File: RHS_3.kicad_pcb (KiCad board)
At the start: 2 copper layers, 51 x 61 mm, 64 parts, among them IC1 ATMEGA328P-A, IC2 CC1101, IC3 CC1101_Chip, J1 Glass Breakage Detector, J2 ANT, P4 ISP Bottom, P5 ISP Top, P6 FTDI, P7 ISP 10, SW1 Reset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

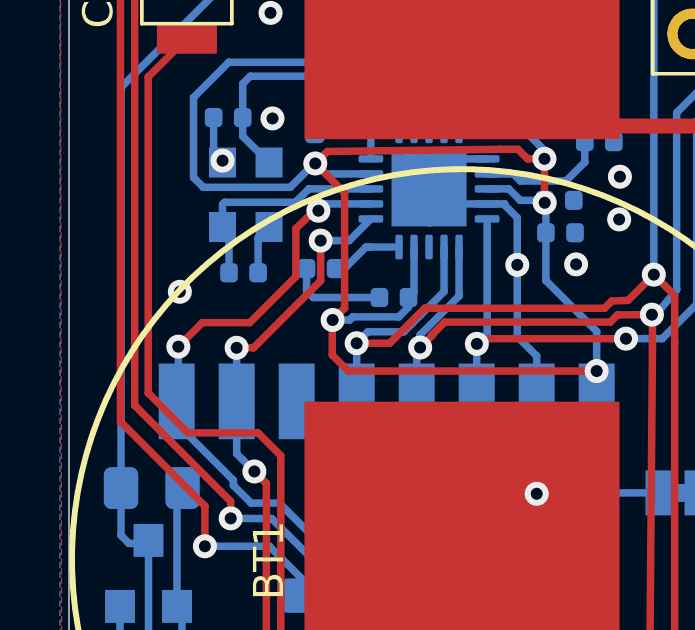
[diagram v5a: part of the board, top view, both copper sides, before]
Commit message: layout changed
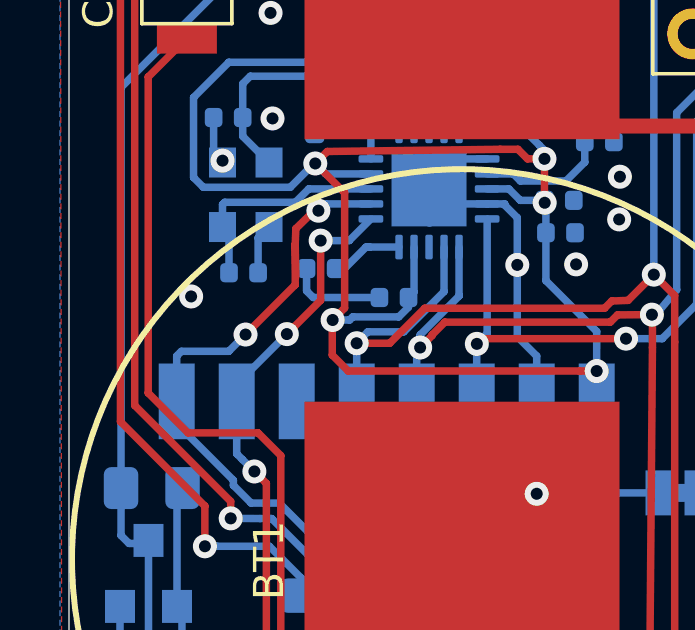
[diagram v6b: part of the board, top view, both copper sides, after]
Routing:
- net /CS: track 31.1 -> 32.3 mm
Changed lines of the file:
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@@
     (thickness 1.6)
     (drawings 33)
-    (tracks 713)
+    (tracks 717)
     (zones 0)
     (modules 64)
@@
     (tags "solder jumper open")
     (attr virtual)
-    (fp_text reference JP2 (at 0 1.8) (layer B.SilkS)
+    (fp_text reference JP2 (at 3.0734 -0.01016) (layer B.SilkS)
       (effects (font (size 1 1) (thickness 0.15)) (justify mirror))
     )
@@
   (segment (start 71.501 88.1888) (end 71.5137 88.2015) (width 0.25) (layer B.Cu) (net 2))
   (segment (start 71.501 87.0585) (end 71.501 87.1093) (width 0.25) (layer B.Cu) (net 2))
-  (via (at 63.1952 90.4875) (size 0.8) (drill 0.4) (layers F.Cu B.Cu) (net 2))
+  (via (at 63.57112 90.64244) (size 0.8) (drill 0.4) (layers F.Cu B.Cu) (net 2))
   (via (at 77.8637 86.6521) (size 0.8) (drill 0.4) (layers F.Cu B.Cu) (net 2))
   (via (at 77.8383 88.0745) (size 0.8) (drill 0.4) (layers F.Cu B.Cu) (net 2))
@@
   (segment (start 69.68 99.03) (end 70.7 100.05) (width 0.25) (layer B.Cu) (net 34))
   (segment (start 71.423599 103.520009) (end 71.796401 103.520009) (width 0.25) (layer B.Cu) (net 34))
-  (via (at 63.1444 92.3163) (size 0.8) (drill 0.4) (layers F.Cu B.Cu) (net 34))
+  (via (at 65.38468 91.91244) (size 0.8) (drill 0.4) (layers F.Cu B.Cu) (net 34))
   (segment (start 63.1444 94.0856) (end 63.09 94.14) (width 0.25) (layer B.Cu) (net 34))
-  (segment (start 63.1444 92.3163) (end 63.1444 94.0856) (width 0.25) (layer B.Cu) (net 34))
   (segment (start 68.038345 87.5585) (end 67.813335 87.78351) (width 0.25) (layer B.Cu) (net 34))
   (segment (start 69.5635 87.5585) (end 68.038345 87.5585) (width 0.25) (layer B.Cu) (net 34))
   (segment (start 67.813335 87.761653) (end 67.813335 87.78351) (width 0.25) (layer B.Cu) (net 34))
   (segment (start 67.67719 87.78351) (end 67.813335 87.78351) (width 0.25) (layer F.Cu) (net 34))
-  (via (at 67.813335 87.78351) (size 0.8) (drill 0.4) (layers F.Cu B.Cu) (net 34))
+  (via (at 67.813335 87.78351) (size 0.8) (drill 0.4) (layers F.Cu B.Cu) (net 34) (status 1000000))
   (segment (start 67.866488 87.7085) (end 67.813335 87.761653) (width 0.25) (layer B.Cu) (net 34))
-  (segment (start 63.94577 91.51493) (end 65.52819 91.51493) (width 0.25) (layer F.Cu) (net 34))
-  (segment (start 63.1444 92.3163) (end 63.94577 91.51493) (width 0.25) (layer F.Cu) (net 34))
-  (segment (start 67.06108 89.98204) (end 67.06108 88.38184) (width 0.25) (layer F.Cu) (net 34))
-  (segment (start 65.52819 91.51493) (end 67.06108 89.98204) (width 0.25) (layer F.Cu) (net 34))
   (segment (start 67.06108 88.38184) (end 67.67719 87.78351) (width 0.25) (layer F.Cu) (net 34))
+  (segment (start 67.06108 89.98204) (end 67.04076 88.90508) (width 0.25) (layer F.Cu) (net 34))
+  (segment (start 67.04076 88.90508) (end 67.06108 88.38184) (width 0.25) (layer F.Cu) (net 34))
+  (segment (start 63.24676 92.47124) (end 64.82588 92.47124) (width 0.25) (layer B.Cu) (net 34))
+  (segment (start 63.09 94.14) (end 63.09 92.628) (width 0.25) (layer B.Cu) (net 34))
+  (segment (start 64.82588 92.47124) (end 65.38468 91.91244) (width 0.25) (layer B.Cu) (net 34))
+  (segment (start 63.09 92.628) (end 63.24676 92.47124) (width 0.25) (layer B.Cu) (net 34))
+  (segment (start 67.04076 90.25636) (end 65.38468 91.91244) (width 0.25) (layer F.Cu) (net 34))
+  (segment (start 67.04076 88.90508) (end 67.04076 90.25636) (width 0.25) (layer F.Cu) (net 34))
   (segment (start 71.84 113.3) (end 71.84 110.652354) (width 0.25) (layer B.Cu) (net 35))
   (via (at 72.015431 110.476923) (size 0.8) (drill 0.4) (layers F.Cu B.Cu) (net 35))
@@
   (via (at 65.67971 96.476464) (size 0.8) (drill 0.4) (layers F.Cu B.Cu) (net 35))
   (segment (start 65.09 94.14) (end 65.09 95.886754) (width 0.25) (layer B.Cu) (net 35))
-  (via (at 65.0875 92.3544) (size 0.8) (drill 0.4) (layers F.Cu B.Cu) (net 35))
+  (via (at 66.76136 91.8972) (size 0.8) (drill 0.4) (layers F.Cu B.Cu) (net 35))
   (segment (start 65.0875 94.1375) (end 65.09 94.14) (width 0.25) (layer B.Cu) (net 35))
-  (segment (start 65.0875 92.3544) (end 65.0875 94.1375) (width 0.25) (layer B.Cu) (net 35))
   (segment (start 69.5635 88.0585) (end 68.841314 88.780686) (width 0.25) (layer B.Cu) (net 35))
   (via (at 67.888589 88.780686) (size 0.8) (drill 0.4) (layers F.Cu B.Cu) (net 35))
   (segment (start 68.841314 88.780686) (end 67.888589 88.780686) (width 0.25) (layer B.Cu) (net 35))
-  (segment (start 67.888589 90.118996) (end 67.888589 89.346371) (width 0.25) (layer F.Cu) (net 35))
-  (segment (start 67.888589 89.346371) (end 67.888589 88.780686) (width 0.25) (layer F.Cu) (net 35))
-  (segment (start 65.653185 92.3544) (end 67.888589 90.118996) (width 0.25) (layer F.Cu) (net 35))
-  (segment (start 65.0875 92.3544) (end 65.653185 92.3544) (width 0.25) (layer F.Cu) (net 35))
+  (segment (start 65.09 93.478) (end 65.09 94.14) (width 0.25) (layer B.Cu) (net 35))
+  (segment (start 65.09 94.14) (end 65.09 93.41108) (width 0.25) (layer B.Cu) (net 35))
+  (segment (start 65.24748 93.41108) (end 66.76136 91.8972) (width 0.25) (layer B.Cu) (net 35))
+  (segment (start 65.09 93.41108) (end 65.24748 93.41108) (width 0.25) (layer B.Cu) (net 35))
+  (segment (start 67.888589 90.769971) (end 66.76136 91.8972) (width 0.25) (layer F.Cu) (net 35))
+  (segment (start 67.888589 88.780686) (end 67.888589 90.769971) (width 0.25) (layer F.Cu) (net 35))
   (segment (start 71.001 83.805) (end 70.5485 83.3525) (width 0.25) (layer B.Cu) (net 37))
   (segment (start 71.001 85.121) (end 71.001 83.805) (width 0.25) (layer B.Cu) (net 37))

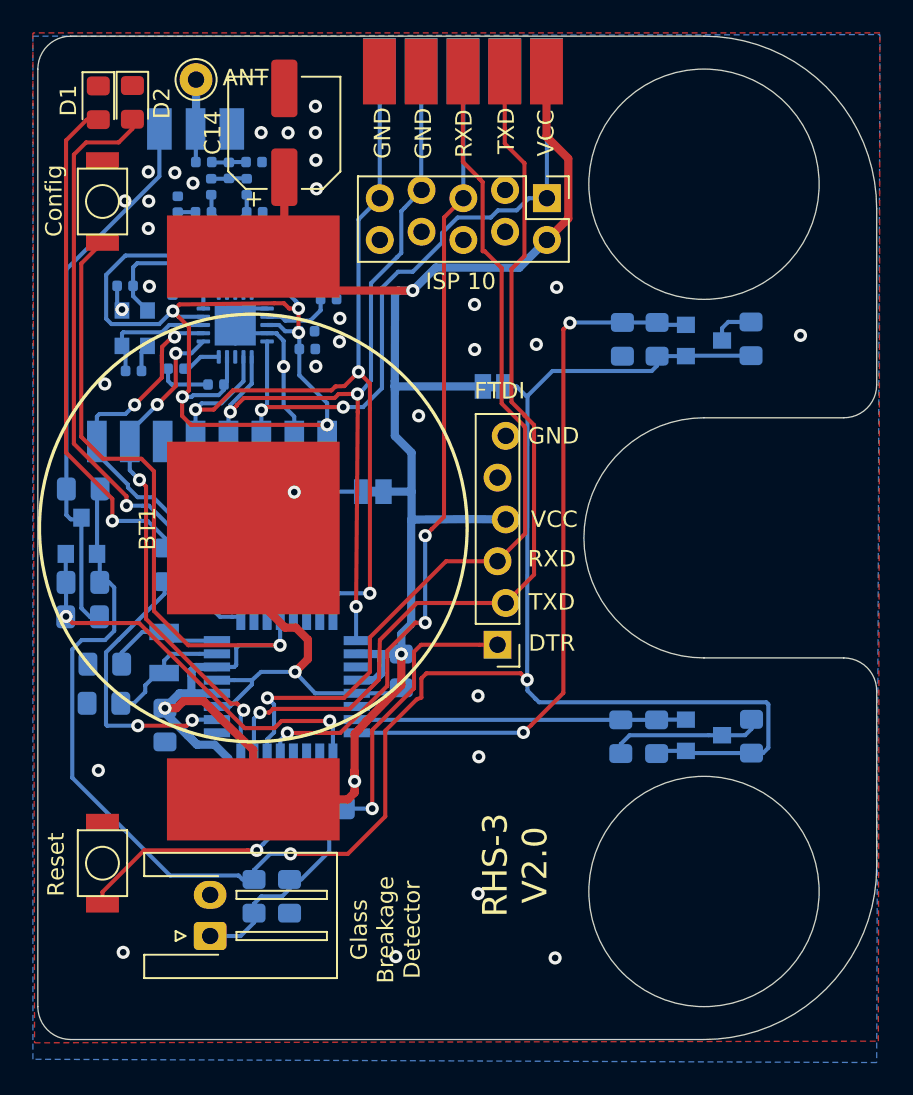
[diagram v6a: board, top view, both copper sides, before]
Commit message: switches for TLEs & CC1101 added
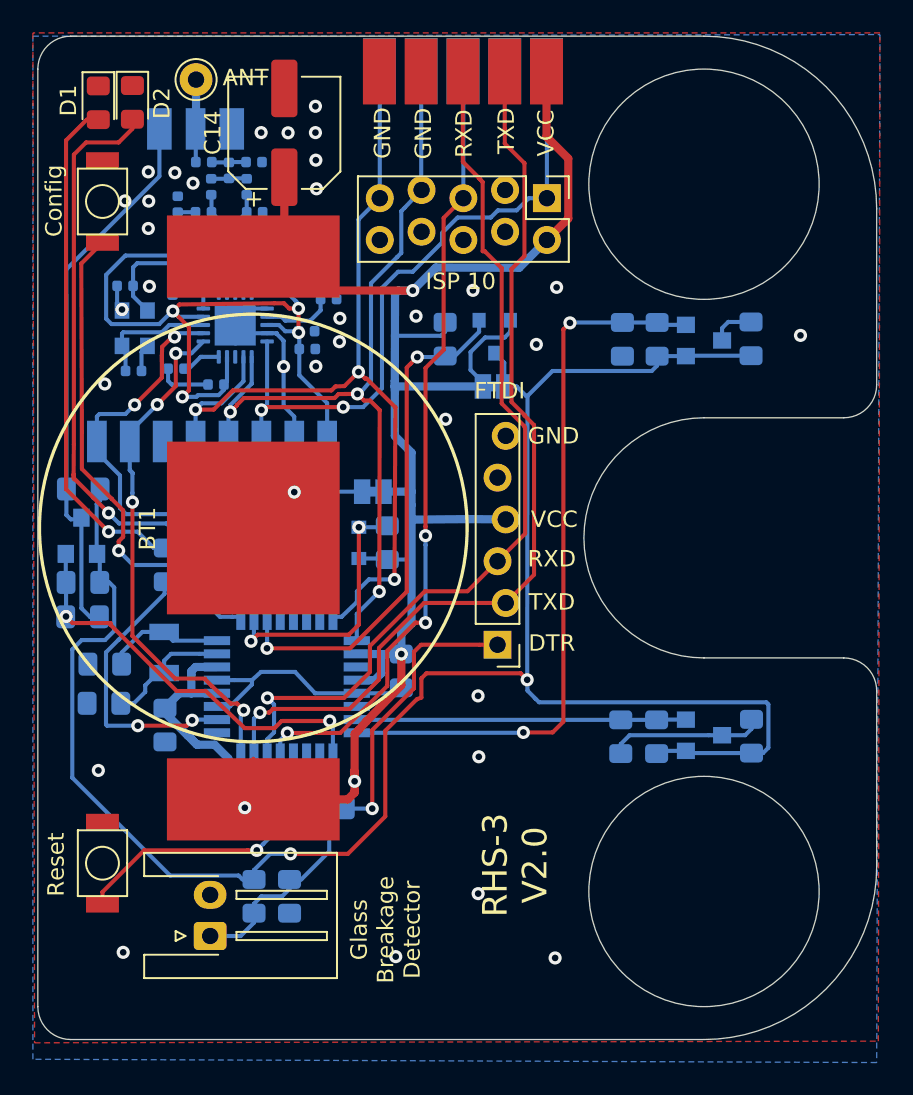
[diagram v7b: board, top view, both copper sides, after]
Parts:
- added Q1: Si2305CDS, Package_TO_SOT_SMD:SOT-23, B.Cu at (78.0, 100.3)
- added Q2: Si2305CDS, Package_TO_SOT_SMD:SOT-23, B.Cu at (87.3, 87.8)
- added R10: 10k, Resistor_SMD:R_0805_2012Metric_Pad1.15x1.40mm_HandSolder, B.Cu at (84.3, 87.9)
- added R9: 10k, Resistor_SMD:R_0805_2012Metric_Pad1.15x1.40mm_HandSolder, B.Cu at (80.7, 100.3)
- C27: value 1p5 -> 100n
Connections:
- net VSS renamed VDC
- IC1 pad 11: Net-(IC1-Pad11) -> /D7
- IC1 pad 12: VCC -> Net-(IC1-Pad12)
- SW2 pad 1: VCC -> Net-(IC1-Pad12)
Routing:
- net VCC: track 176.5 -> 138.1 mm, vias 5 -> 4
- net Net-(IC1-Pad12): track 0.00 -> 32.5 mm, vias 0 -> 1
- net /D7: track 0.00 -> 31.5 mm, vias 0 -> 2
- net /D6: track 0.00 -> 16.2 mm, vias 0 -> 2
- net VDC: track 72.1 -> 65.0 mm, vias 5 -> 4
- net GND: track 90.3 -> 83.6 mm, vias 34 -> 33
- net /MOSI: track 57.4 -> 54.7 mm
- net VDD: track 119.1 -> 121.4 mm
- net /MISO: track 54.0 -> 55.4 mm
- net /SCK: track 50.1 -> 51.4 mm
- net /GDO0: track 31.6 -> 32.9 mm
- net Net-(D2-Pad2): track 34.0 -> 35.2 mm
- net /A1: track 43.5 -> 44.6 mm
- net /CS: track 32.3 -> 31.7 mm

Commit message: layout updates
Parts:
- moved R10 1.83 mm to (84.2, 89.7), turned to 90 degrees
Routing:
- net VCC: track 138.1 -> 133.0 mm, vias 4 -> 5
- net GND: track 83.6 -> 86.4 mm, vias 33 -> 38
- net /RXD: track 54.5 -> 56.1 mm, vias 1 -> 3
- net /SCK: track 51.4 -> 52.5 mm
- net /A1: track 44.6 -> 43.5 mm
- net /MISO: track 55.4 -> 54.4 mm
- net Net-(IC1-Pad12): track 32.5 -> 33.3 mm
- net /RESET: track 68.0 -> 68.7 mm
- net /MOSI: track 54.7 -> 54.1 mm
- net /TXD: vias 1 -> 3
